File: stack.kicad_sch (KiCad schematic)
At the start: 108 parts, among them CN1 10nF, CN2 10nF, CN3 10nF, CN4 10nF, CN5 10nF, CN6 10nF, CN7 10nF, J5 CELLS, J6 TEMP0, J7 TEMP1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

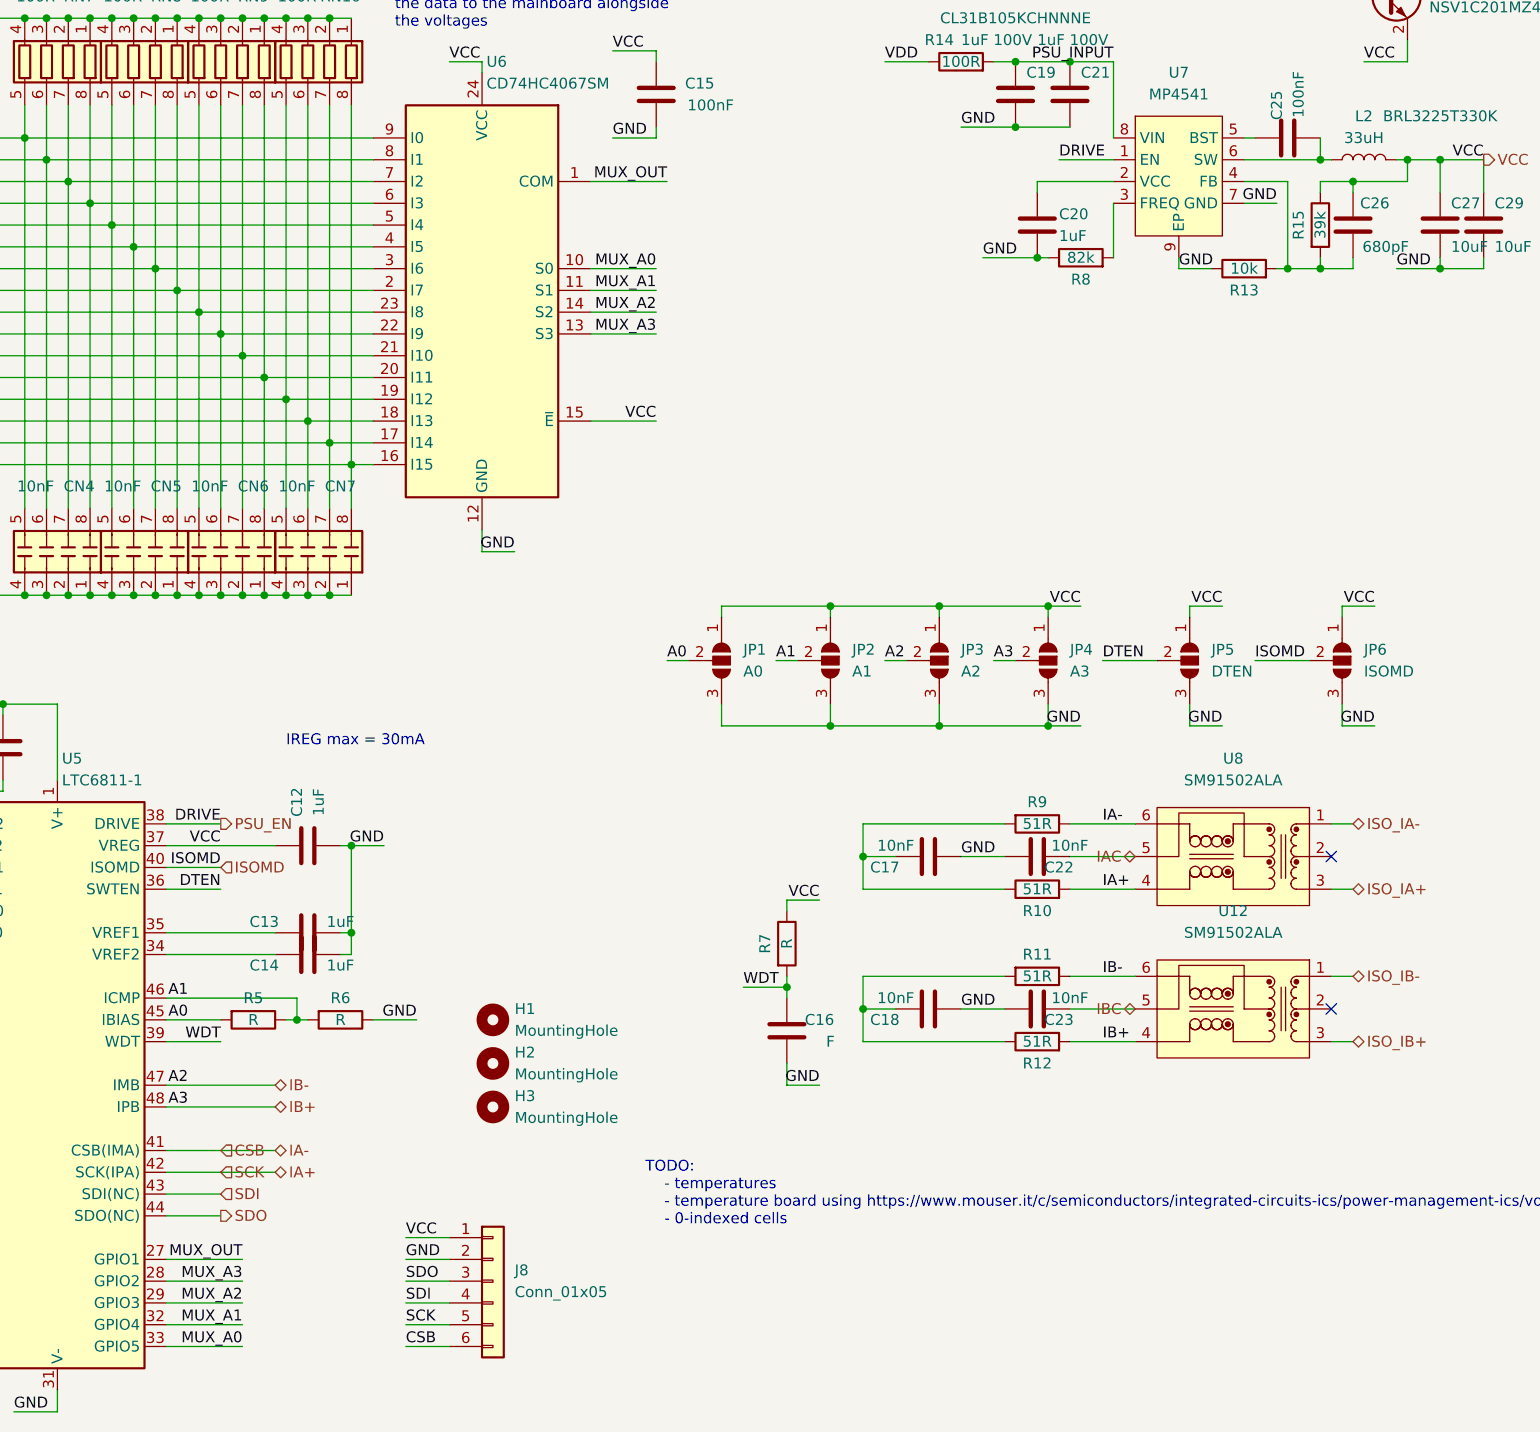
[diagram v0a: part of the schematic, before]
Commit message: Fixed issure #2
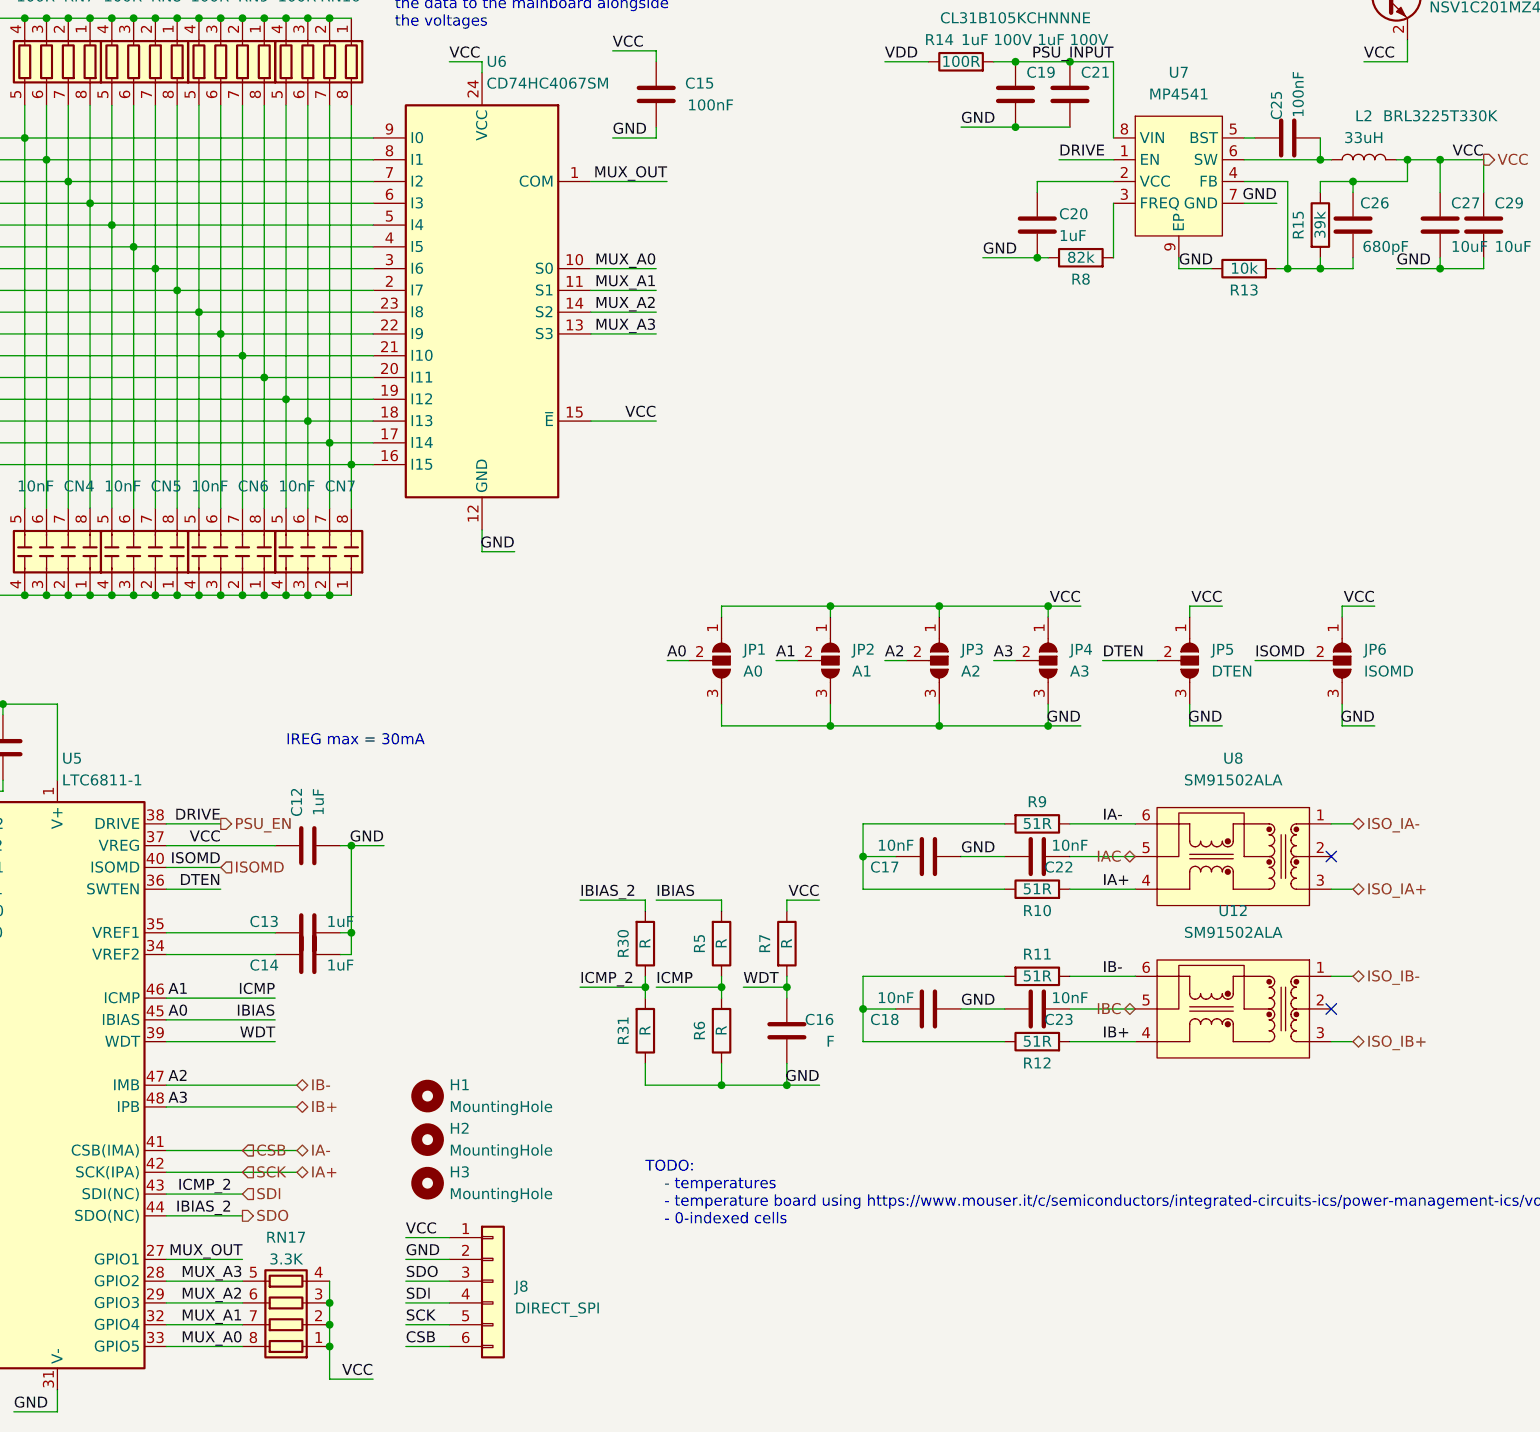
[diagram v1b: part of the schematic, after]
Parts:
- added R30, R31: R, Resistor_SMD:R_0603_1608Metric, symbol Device:R
- added RN17: 3.3K, Resistor_SMD:R_Array_Convex_4x0603, symbol Device:R_Pack04
- J8: value Conn_01x05 -> DIRECT_SPI
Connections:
- net GND: now also R31.1
- net MUX_A0: now also RN17.8 (R1.2)
- net MUX_A1: now also RN17.7 (R2.2)
- net MUX_A2: now also RN17.6 (R3.2)
- net MUX_A3: now also RN17.5 (R4.2)
- net SDI: now also R30.1, R31.2
- net SDO: now also R30.2
- net VCC: now also RN17.1 (R1.1), RN17.2 (R2.1), RN17.3 (R3.1), RN17.4 (R4.1)
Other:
- moved on the sheet: H1, H2, H3, R5, R6

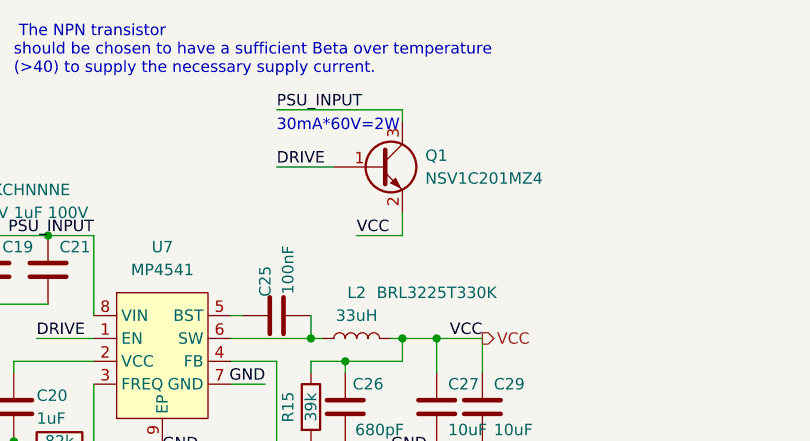
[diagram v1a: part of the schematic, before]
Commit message: addressed swapped collector emitter of Q1
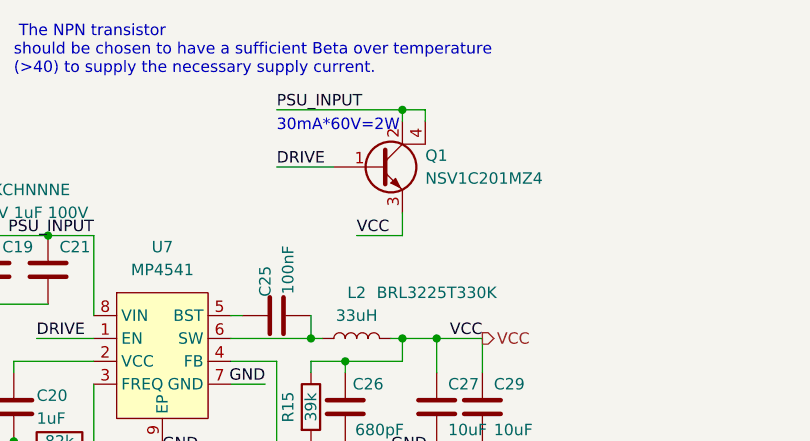
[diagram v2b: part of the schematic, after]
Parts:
- Q1: footprint Package_TO_SOT_SMD:SOT-223-3_TabPin2 -> Package_TO_SOT_SMD:SOT-223; symbol Device:Q_NPN_BEC -> Device:Q_NPN_BCEC
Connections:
- net PSU_INPUT: now also Q1.2 (C), Q1.4 (C); no longer Q1.3 (C)
- net VCC: now also Q1.3 (E); no longer Q1.2 (E)
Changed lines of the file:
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@@
   (junction (at 140.97 101.6) (diameter 0) (color 0 0 0 0)
+  )
+  (junction (at 266.7 25.4) (diameter 0) (color 0 0 0 0)
   )
   (no_connect (at 55.88 19.05))
@@
     (stroke (width 0) (type default))
   )
+  (wire (pts (xy 269.24 25.4) (xy 269.24 26.67))
+    (stroke (width 0) (type default))
+  )
   (wire (pts (xy 91.44 171.45) (xy 96.52 171.45))
     (stroke (width 0) (type default))
@@
   )
   (wire (pts (xy 115.57 58.42) (xy 146.05 58.42))
+    (stroke (width 0) (type default))
+  )
+  (wire (pts (xy 266.7 25.4) (xy 269.24 25.4))
     (stroke (width 0) (type default))
   )
@@
     (effects (font (size 1.27 1.27)) (justify left))
   )
-  (symbol (lib_id "Device:Q_NPN_BEC") (at 264.16 31.75 0) (unit 1)
+  (symbol (lib_id "Device:Q_NPN_BCEC") (at 264.16 31.75 0) (unit 1)
     (in_bom yes) (on_board yes) (dnp no) (fields_autoplaced)
     (property "Reference" "Q1" (at 269.24 30.4799 0)
@@
       (effects (font (size 1.27 1.27)) (justify left))
     )
-    (property "Footprint" "Package_TO_SOT_SMD:SOT-223-3_TabPin2" (at 269.24 29.21 0)
+    (property "Footprint" "Package_TO_SOT_SMD:SOT-223" (at 269.24 29.21 0)
       (effects (font (size 1.27 1.27)) hide)
     )
@@
     (pin "2")
     (pin "3")
+    (pin "4")
     (instances
       (project "bms_monitor"

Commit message: changed to bigger footprint for HV caps
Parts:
- C11, C19, C21: footprint Capacitor_SMD:C_1206_3216Metric -> Capacitor_SMD:C_1210_3225Metric
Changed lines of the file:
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@@
       (effects (font (size 1.27 1.27)) (justify left))
     )
-    (property "Footprint" "Capacitor_SMD:C_1206_3216Metric" (at 221.9452 46.99 0)
+    (property "Footprint" "Capacitor_SMD:C_1210_3225Metric" (at 221.9452 46.99 0)
       (effects (font (size 1.27 1.27)) hide)
     )
@@
       (effects (font (size 1.27 1.27)) (justify left))
     )
-    (property "Footprint" "Capacitor_SMD:C_1206_3216Metric" (at 228.2952 46.99 0)
+    (property "Footprint" "Capacitor_SMD:C_1210_3225Metric" (at 228.2952 46.99 0)
       (effects (font (size 1.27 1.27)) hide)
     )
@@
       (effects (font (size 1.27 1.27)) (justify left))
     )
-    (property "Footprint" "Capacitor_SMD:C_1206_3216Metric" (at 103.8352 123.19 0)
-      (effects (font (size 1.27 1.27)) hide)
-    )
+    (property "Footprint" "Capacitor_SMD:C_1210_3225Metric" (at 103.8352 123.19 0)
+      (effects (font (size 1.27 1.27)) hide)
+    )

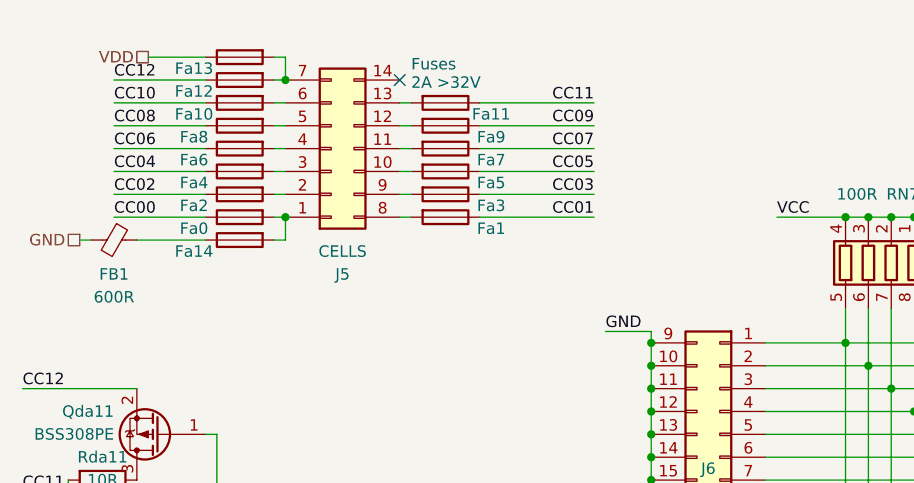
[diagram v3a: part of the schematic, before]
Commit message: added different VDD pin for external supply
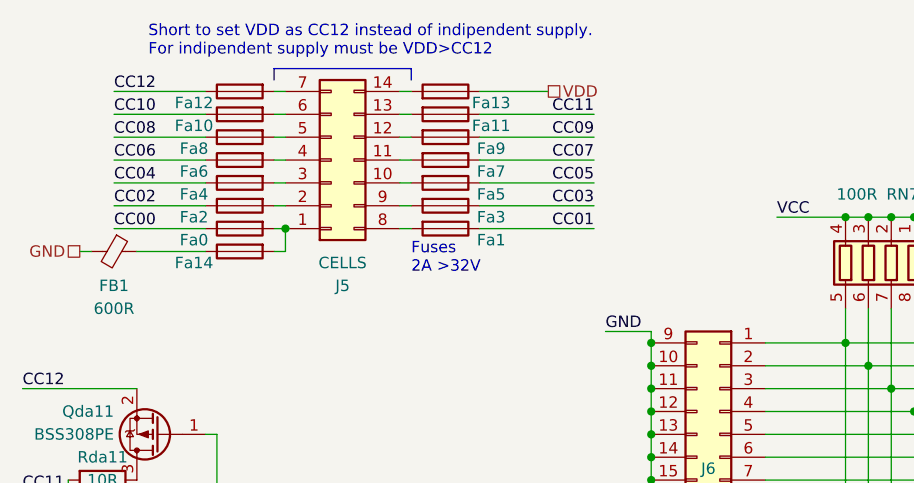
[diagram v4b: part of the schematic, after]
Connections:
- net at Fa12.2, J5.7 (Pin_7): no longer Fa13.2
- net at J5.14 (Pin_14): now also Fa13.2
- no-connect marks 3 -> 2
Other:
- note added: "Short to set VDD as CC12 instead of indipendent supply. For indipendent supply must be VDD>CC12"
- moved on the sheet: FB1, Fa0, Fa1, Fa10, Fa11, Fa12, Fa13, Fa14, Fa2, Fa3, Fa4, Fa5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

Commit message: fixed enable mux
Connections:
- net GND: now also U6.15 (~{E})
- net VCC: no longer U6.15 (~{E})
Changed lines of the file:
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@@
     (effects (font (size 1.27 1.27)) (justify left bottom))
+  )
+  (label "GND" (at 179.07 81.28 180) (fields_autoplaced)
+    (effects (font (size 1.27 1.27)) (justify right bottom))
   )
   (label "C04" (at 80.01 115.57 180) (fields_autoplaced)
@@
     (effects (font (size 1.27 1.27)) (justify left bottom))
   )
-  (label "VCC" (at 179.07 81.28 180) (fields_autoplaced)
-    (effects (font (size 1.27 1.27)) (justify right bottom))
-  )
   (label "C05" (at 59.69 161.29 0) (fields_autoplaced)
